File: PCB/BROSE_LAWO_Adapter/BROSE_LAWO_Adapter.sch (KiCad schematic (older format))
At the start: 7 parts, among them J1 LAWO Controller, J2 BROSE, J3 24V

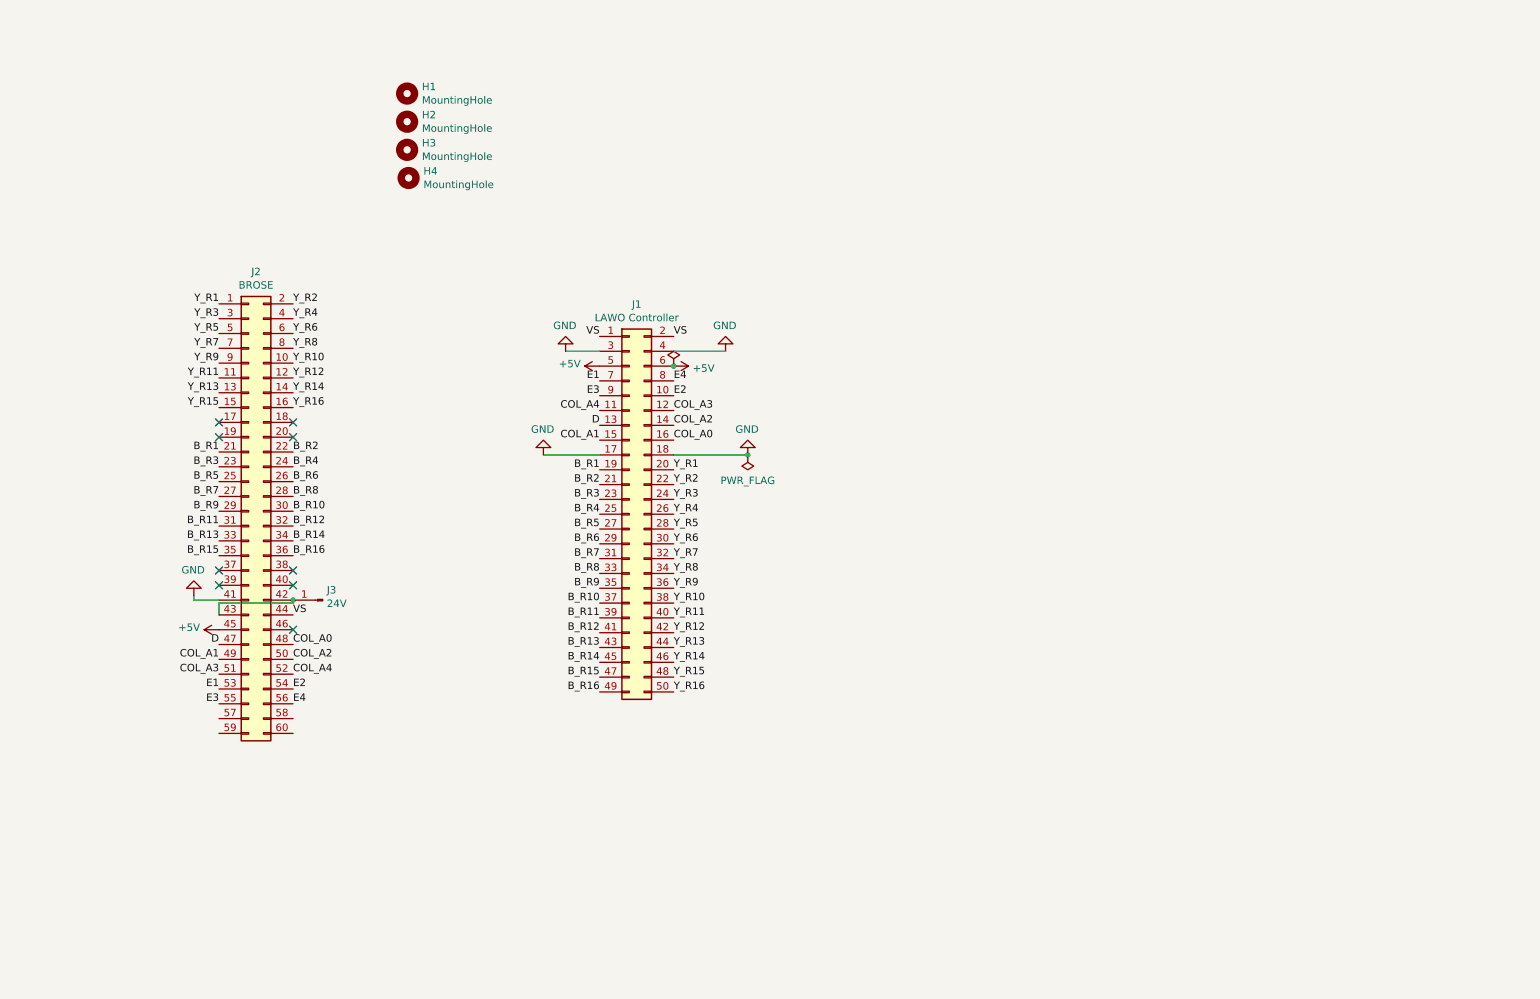
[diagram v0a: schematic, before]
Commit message: update BROSE_LAWO Adapter PCB
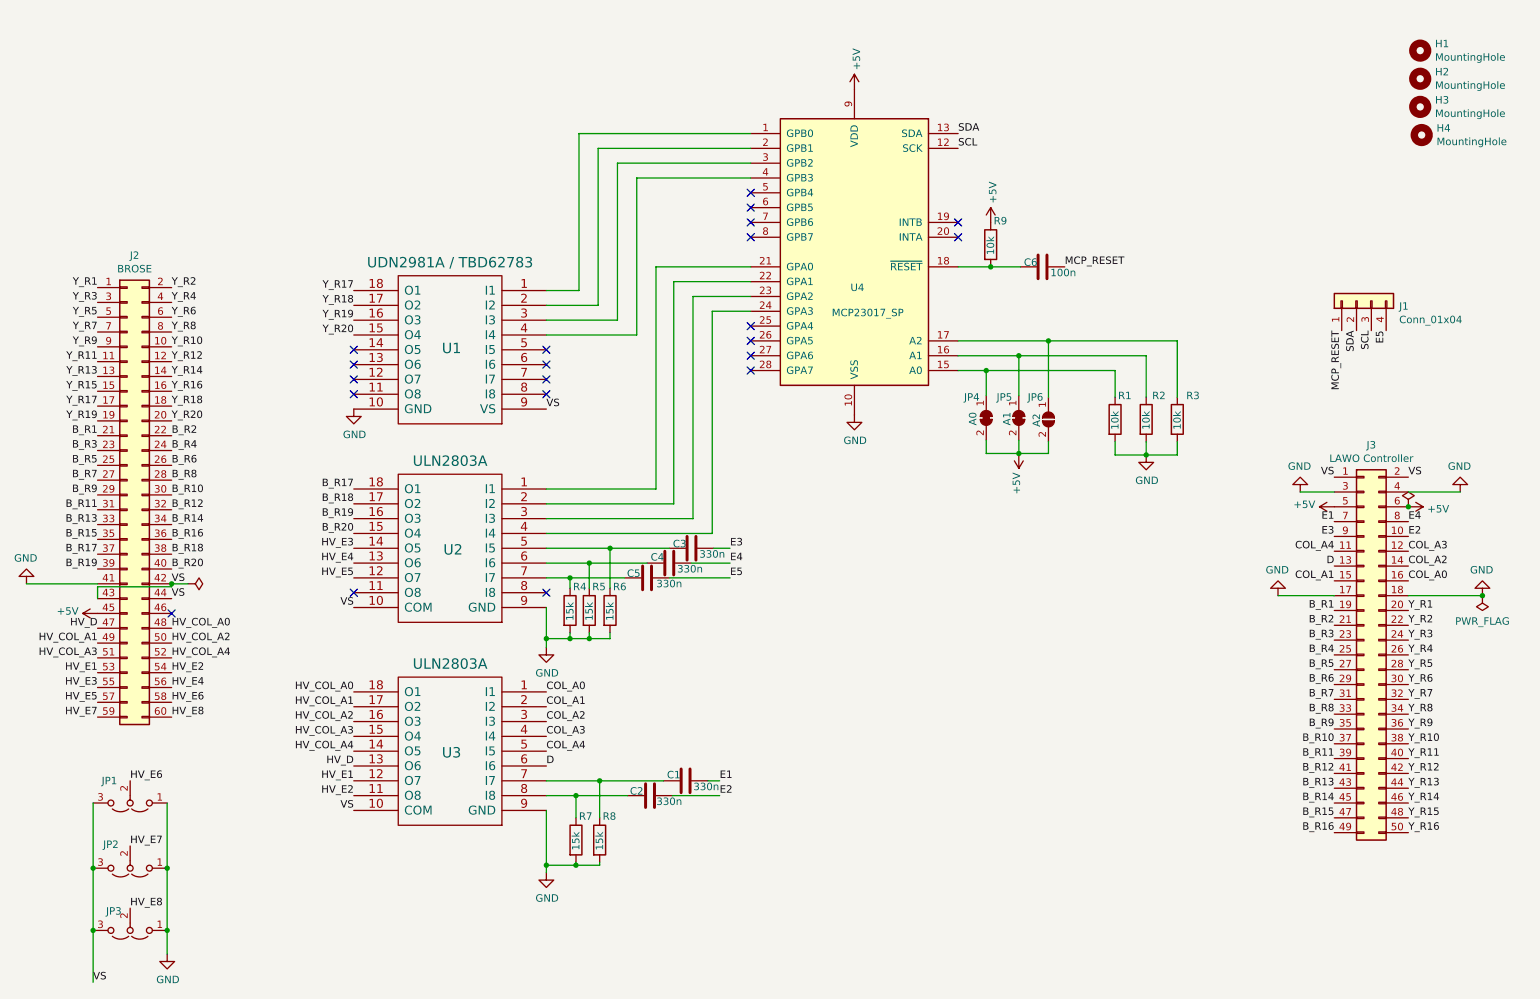
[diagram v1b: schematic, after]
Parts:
- removed J3: 24V, Connector_PinHeader_2.54mm:PinHeader_1x01_P2.54mm_Vertical, symbol Connector:Conn_01x01_Male
- added C1, C2, C3, C4, C5: 330n, Capacitor_THT:C_Rect_L10.0mm_W4.0mm_P7.50mm_MKS4, symbol Device:C
- added C6: 100n, Capacitor_SMD:C_0805_2012Metric_Pad1.15x1.40mm_HandSolder, symbol Device:C
- added J1: Conn_01x04, Connector_PinHeader_2.54mm:PinHeader_1x04_P2.54mm_Vertical, symbol Connector_Generic:Conn_01x04
- added JP1: E6, Connector_PinHeader_2.54mm:PinHeader_1x03_P2.54mm_Vertical, symbol Jumper:Jumper_3_Open
- added JP2: E7, Connector_PinHeader_2.54mm:PinHeader_1x03_P2.54mm_Vertical, symbol Jumper:Jumper_3_Open
- added JP3: E8, Connector_PinHeader_2.54mm:PinHeader_1x03_P2.54mm_Vertical, symbol Jumper:Jumper_3_Open
- added JP4: A0, Jumper:SolderJumper-2_P1.3mm_Bridged_RoundedPad1.0x1.5mm, symbol Jumper:SolderJumper_2_Bridged
- added JP5: A1, Jumper:SolderJumper-2_P1.3mm_Bridged_RoundedPad1.0x1.5mm, symbol Jumper:SolderJumper_2_Bridged
- added JP6: A2, Jumper:SolderJumper-2_P1.3mm_Open_RoundedPad1.0x1.5mm, symbol Jumper:SolderJumper_2_Open
- added R1, R2, R3, R9: 10k, Resistor_SMD:R_0805_2012Metric_Pad1.15x1.40mm_HandSolder, symbol Device:R
- added R4, R5, R6, R7, R8: 15k, Resistor_THT:R_Axial_DIN0204_L3.6mm_D1.6mm_P2.54mm_Vertical, symbol Device:R
- added U1: UDN2981A / TBD62783, Package_DIP:DIP-18_W7.62mm_Socket, symbol LAWO_ESP32-rescue:UDN2981A
- added U2, U3: ULN2803A, Package_DIP:DIP-18_W7.62mm_Socket, symbol LAWO_ESP32-rescue:ULN2803A
- added U4: MCP23017_SP, Package_DIP:DIP-28_W7.62mm, symbol Interface_Expansion:MCP23017_SP
- renumbered J1 to J3
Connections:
- net +5V: now also JP4.2 (B), JP5.2 (B), JP6.2 (B), R9.1, U4.9 (VDD)
- net COL_A0: now also U3.1 (I1); no longer J2.48 (Pin_48)
- net COL_A1: now also U3.2 (I2); no longer J2.49 (Pin_49)
- net COL_A2: now also U3.3 (I3); no longer J2.50 (Pin_50)
- net COL_A3: now also U3.4 (I4); no longer J2.51 (Pin_51)
- net COL_A4: now also U3.5 (I5); no longer J2.52 (Pin_52)
- net D: now also U3.6 (I6); no longer J2.47 (Pin_47)
- net E1: now also C1.2; no longer J2.53 (Pin_53)
- net E2: now also C2.2; no longer J2.54 (Pin_54)
- net E3: now also C3.2; no longer J2.55 (Pin_55)
- net E4: now also C4.2; no longer J2.56 (Pin_56)
- net GND: now also JP1.1 (A), JP2.1 (A), JP3.1 (A), R1.2, R2.2, R3.2, R4.2, R5.2, R6.2, R7.2, R8.2, U1.10 (GND), U2.9 (GND), U3.9 (GND), U4.10 (VSS)
- net VS: now also J2.42 (Pin_42), J2.43 (Pin_43), JP1.3 (B), JP2.3 (B), JP3.3 (B), U1.9 (VS), U2.10 (COM), U3.10 (COM)
- net Y_R17: now reaches J2.17 (Pin_17)
- net Y_R17: now also U1.18 (O1)
- net Y_R18: now reaches J2.18 (Pin_18)
- net Y_R18: now also U1.17 (O2)
- net Y_R19: now reaches J2.19 (Pin_19)
- net Y_R19: now also U1.16 (O3)
- net Y_R20: now reaches J2.20 (Pin_20)
- net Y_R20: now also U1.15 (O4)
- net B_R17: now reaches J2.37 (Pin_37)
- net B_R17: now also U2.18 (O1)
- net B_R18: now reaches J2.38 (Pin_38)
- net B_R18: now also U2.17 (O2)
- net B_R19: now reaches J2.39 (Pin_39)
- net B_R19: now also U2.16 (O3)
- net B_R20: now reaches J2.40 (Pin_40)
- net B_R20: now also U2.15 (O4)
- net HV_E5: now reaches J2.57 (Pin_57)
- net HV_E5: now also U2.12 (O7)
- net HV_E6: now reaches J2.58 (Pin_58)
- net HV_E6: now also JP1.2 (C)
- net HV_E7: now reaches J2.59 (Pin_59)
- net HV_E7: now also JP2.2 (C)
- net HV_E8: now reaches J2.60 (Pin_60)
- net HV_E8: now also JP3.2 (C)
- new net: U1.1 (I1), U4.1 (GPB0)
- new net: JP4.1 (A), R1.1, U4.15 (A0)
- new net: JP5.1 (A), R2.1, U4.16 (A1)
- new net: JP6.1 (A), R3.1, U4.17 (A2)
- new net: C6.1, R9.2, U4.18 (~RESET~)
- new net: U1.2 (I2), U4.2 (GPB1)
- new net: U2.1 (I1), U4.21 (GPA0)
- new net: U2.2 (I2), U4.22 (GPA1)
- new net: U2.3 (I3), U4.23 (GPA2)
- new net: U2.4 (I4), U4.24 (GPA3)
- new net: U1.3 (I3), U4.3 (GPB2)
- new net: U1.4 (I4), U4.4 (GPB3)
- new net: C1.1, R8.1, U3.7 (I7)
- new net: C2.1, R7.1, U3.8 (I8)
- new net: C3.1, R6.1, U2.5 (I5)
- new net: C4.1, R5.1, U2.6 (I6)
- new net: C5.1, R4.1, U2.7 (I7)
- new net E5: C5.2, J1.4 (Pin_4)
- new net HV_COL_A0: J2.48 (Pin_48), U3.18 (O1)
- new net HV_COL_A1: J2.49 (Pin_49), U3.17 (O2)
- new net HV_COL_A2: J2.50 (Pin_50), U3.16 (O3)
- new net HV_COL_A3: J2.51 (Pin_51), U3.15 (O4)
- new net HV_COL_A4: J2.52 (Pin_52), U3.14 (O5)
- new net HV_D: J2.47 (Pin_47), U3.13 (O6)
- new net HV_E1: J2.53 (Pin_53), U3.12 (O7)
- new net HV_E2: J2.54 (Pin_54), U3.11 (O8)
- new net HV_E3: J2.55 (Pin_55), U2.14 (O5)
- new net HV_E4: J2.56 (Pin_56), U2.13 (O6)
- new net MCP_RESET: C6.2, J1.1 (Pin_1)
- new net SCL: J1.3 (Pin_3), U4.12 (SCK)
- new net SDA: J1.2 (Pin_2), U4.13 (SDA)
- no-connect marks 9 -> 21
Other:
- moved on the sheet: H1, H2, H3, H4, J2, J3

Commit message: update
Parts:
- removed J1: Conn_01x04, Connector_PinHeader_2.54mm:PinHeader_1x04_P2.54mm_Vertical, symbol Connector_Generic:Conn_01x04
- added J2: LAWO Controller 20p, Connector_IDC:IDC-Header_2x10_P2.54mm_Vertical, symbol Connector_Generic:Conn_02x10_Odd_Even
- added U5, U6: 4049, Package_DIP:DIP-16_W7.62mm_Socket, symbol 4xxx:4049
- H1, H2, H3, H4: footprint MountingHole:MountingHole_2.7mm_Pad -> Connect:1pin
- U4: footprint Package_DIP:DIP-28_W7.62mm -> Package_DIP:DIP-28_W7.62mm_Socket
- renumbered J3 to J1, J2 to J3
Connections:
- net +5V: now also J2.19 (Pin_19), J2.20 (Pin_20), J2.4 (Pin_4), J2.6 (Pin_6), U5.1 (VCC), U6.1 (VCC)
- net COL_A0: now also U5.3; no longer U3.1 (I1)
- net COL_A1: now also U5.5; no longer U3.2 (I2)
- net COL_A2: now also U5.7; no longer U3.3 (I3)
- net COL_A3: now also U5.9; no longer U3.4 (I4)
- net COL_A4: now also U5.11; no longer U3.5 (I5)
- net D: now also U5.14; no longer U3.6 (I6)
- net E1: now also U6.3; no longer C1.2
- net E2: now also U6.5; no longer C2.2
- net E3: now also U6.7; no longer C3.2
- net E4: now also U6.9; no longer C4.2
- net E5: now also J2.9 (Pin_9), U6.11; no longer C5.2
- net GND: now also J2.1 (Pin_1), J2.2 (Pin_2), J2.3 (Pin_3), J2.5 (Pin_5), U5.8 (VSS), U6.8 (VSS)
- net MCP_RESET: now also J2.11 (Pin_11)
- net SCL: now also J2.13 (Pin_13)
- net SDA: now also J2.15 (Pin_15)
- new net: U3.1 (I1), U5.2
- new net: U3.2 (I2), U5.4
- new net: U3.3 (I3), U5.6
- new net: U3.4 (I4), U5.10
- new net: U3.5 (I5), U5.12
- new net: U3.6 (I6), U5.15
- new net: C1.2, U6.2
- new net: C2.2, U6.4
- new net: C3.2, U6.6
- new net: C4.2, U6.10
- new net: C5.2, U6.12
- no-connect marks 21 -> 31
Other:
- moved on the sheet: J1
